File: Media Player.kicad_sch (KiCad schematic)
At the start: 1 part, among them U1 ESP32-S3-WROOM-1

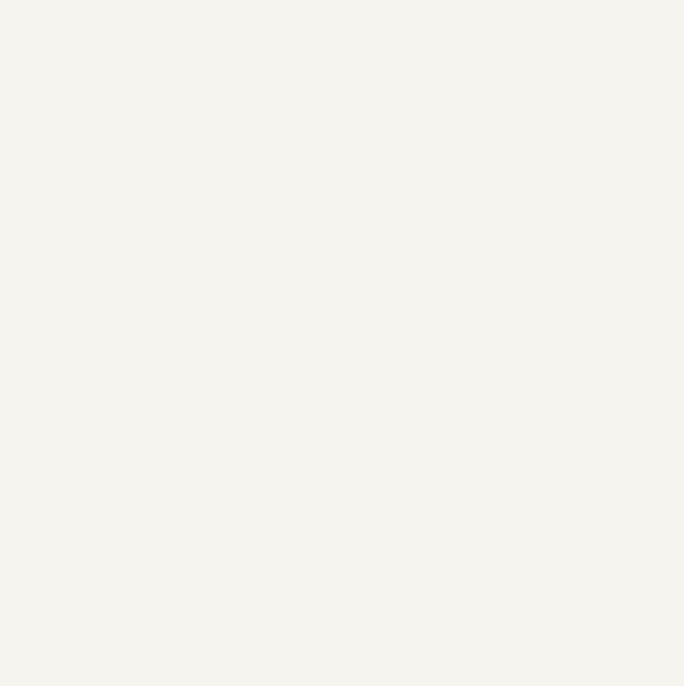
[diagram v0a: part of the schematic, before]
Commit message: Added Power sub page.
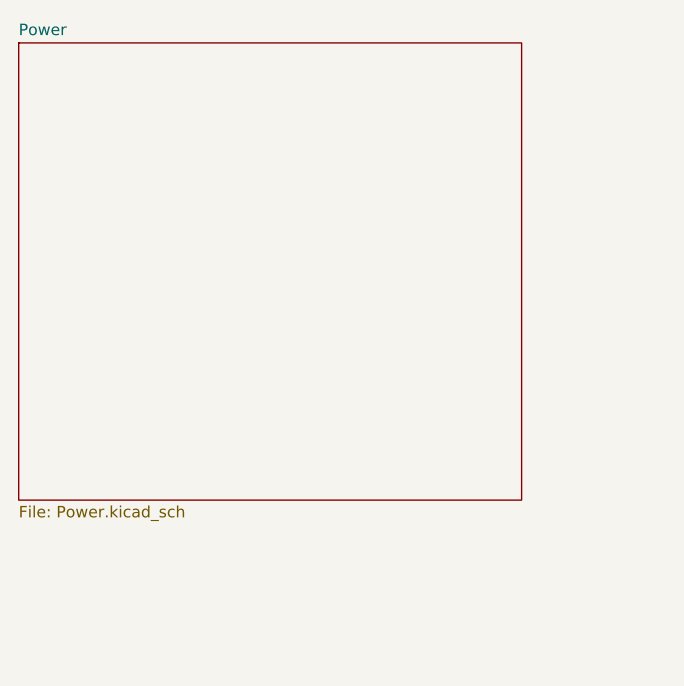
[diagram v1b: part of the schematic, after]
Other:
- added sheet Power (Power.kicad_sch)
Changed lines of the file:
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@@
+		)
+	)
+	(sheet
+		(at 20.32 17.78)
+		(size 55.88 50.8)
+		(exclude_from_sim no)
+		(in_bom yes)
+		(on_board yes)
+		(dnp no)
+		(fields_autoplaced yes)
+		(stroke
+			(width 0.1524)
+			(type solid)
+		)
+		(fill
+			(color 255 248 184 1.0000)
+		)
+		(property "Sheetname" "Power"
+			(at 20.32 17.0684 0)
+			(effects
+				(font
+					(size 1.27 1.27)
+				)
+				(justify left bottom)
+			)
+		)
+		(property "Sheetfile" "Power.kicad_sch"
+			(at 20.32 69.1646 0)
+			(effects
+				(font
+					(size 1.27 1.27)
+				)
+				(justify left top)
+			)
+		)
+		(instances
+			(project "Media Player"
+				(path "/5c19345b-3707-4c90-b593-78a9c3e56866"
+					(page "2")
+				)
+			)
 		)
 	)

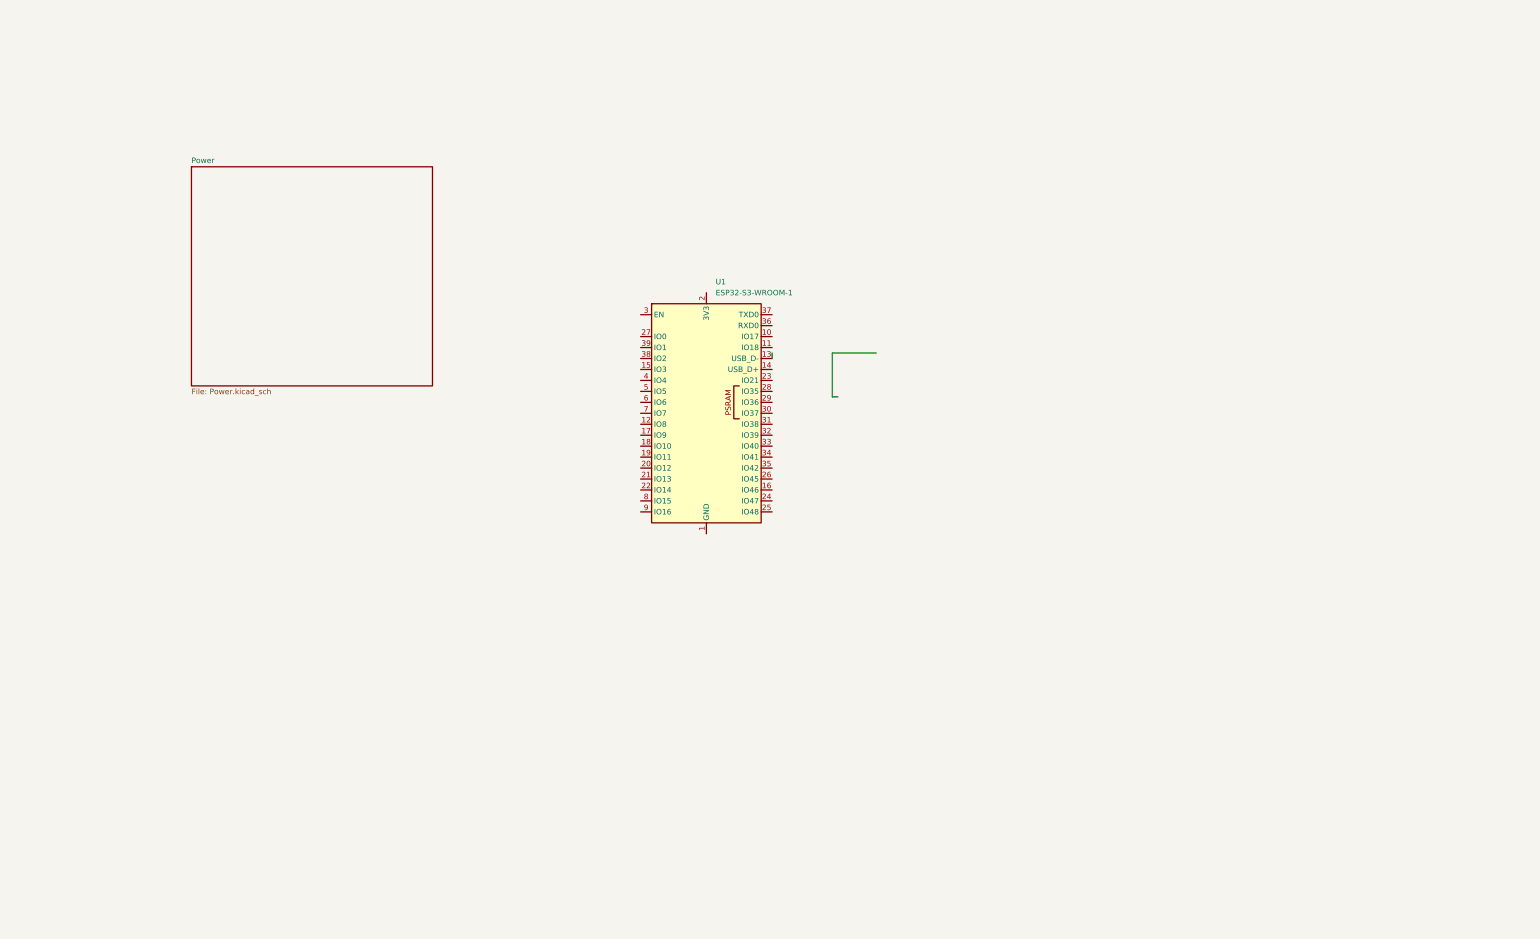
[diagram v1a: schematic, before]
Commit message: Placed Major Components, No Power
Placed ESP32S3, Connector to LCD, SD card reader, USB. Audio Jack components still tbd. Power is a hierarchical page/symbol, no pins right now.
Note to self: KiCAD will crash if you try to edit symbols by double clicking on them inside a schematic. Use symbol editor instead.
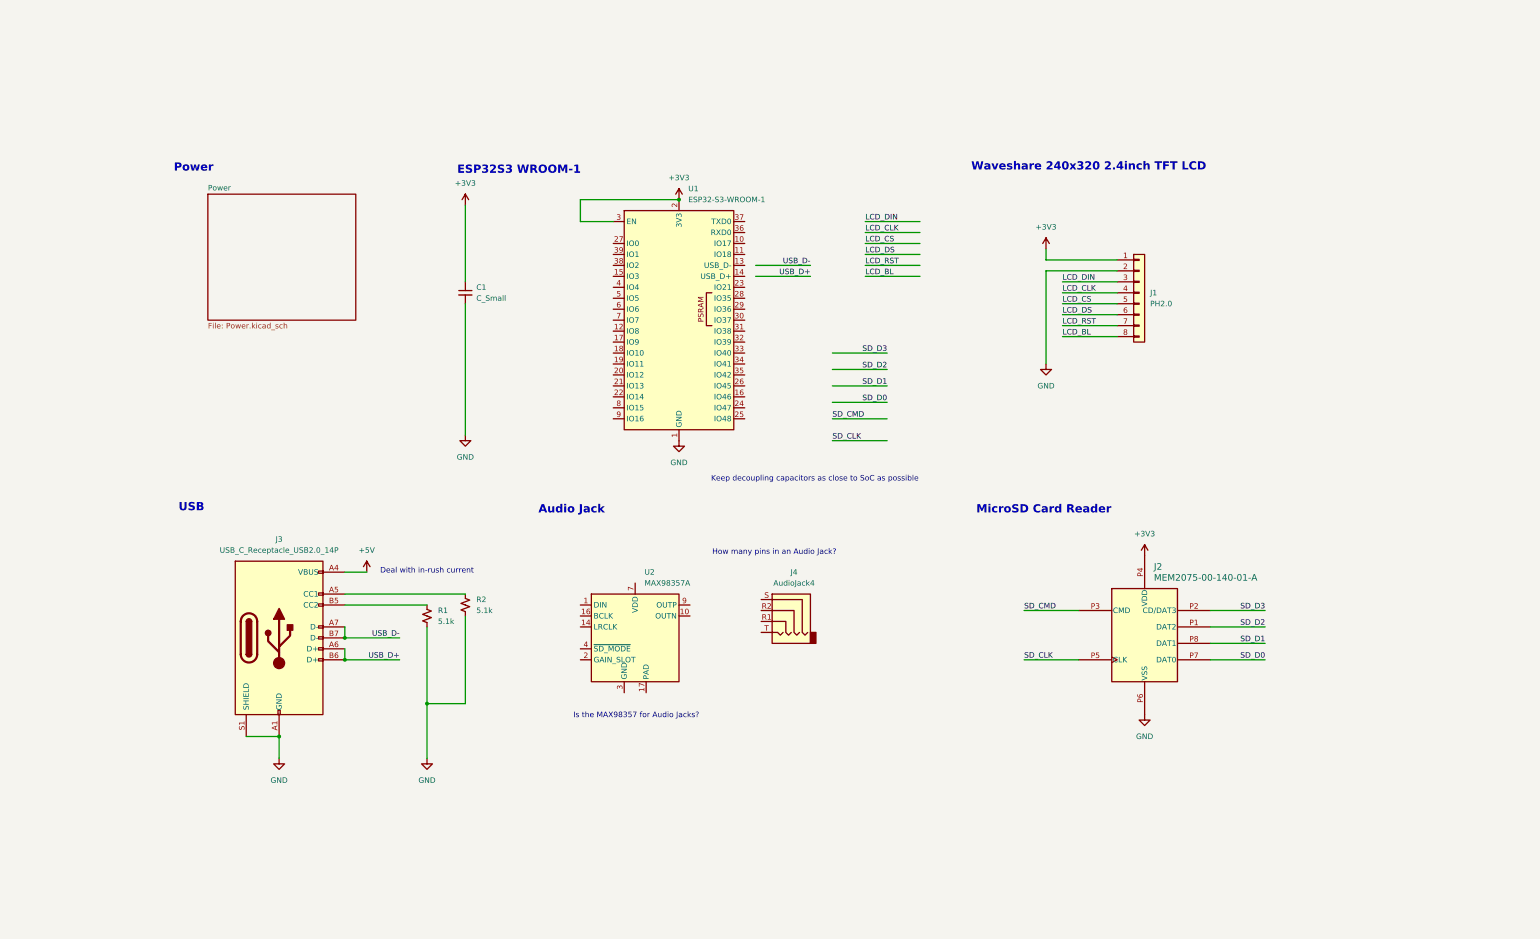
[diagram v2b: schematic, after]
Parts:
- added C1: C_Small, symbol Device:C_Small
- added J1: PH2.0, symbol Connector_Generic:Conn_01x08
- added J2: MEM2075-00-140-01-A, MEM2075-00-140-01-A_GCT, symbol MEM2075:MEM2075-00-140-01-A
- added J3: USB_C_Receptacle_USB2.0_14P, symbol Connector:USB_C_Receptacle_USB2.0_14P
- added J4: AudioJack4, symbol Connector_Audio:AudioJack4
- added R1, R2: 5.1k, symbol Device:R_Small_US
- added U2: MAX98357A, Package_DFN_QFN:TQFN-16-1EP_3x3mm_P0.5mm_EP1.23x1.23mm, symbol Audio:MAX98357A
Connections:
- net GND: now reaches U1.1 (GND), U1.40 (GND), U1.41 (GND)
- net GND: now also C1.2, J1.2 (Pin_2), J2.P6 (VSS), J3.A1 (GND), J3.A12 (GND), J3.B1 (GND), J3.B12 (GND), J3.S1 (SHIELD), R1.2, R2.2
- net +3V3: now reaches U1.2 (3V3)
- net +3V3: now also U1.3 (EN), C1.1, J1.1 (Pin_1), J2.P4 (VDD)
- new net: J3.B5 (CC2), R1.1
- new net: U2.11 (GND), U2.15 (GND), U2.3 (GND)
- new net: U2.7 (VDD), U2.8 (VDD)
- new net: J3.A5 (CC1), R2.1
- new net +5V: J3.A4 (VBUS), J3.A9 (VBUS), J3.B4 (VBUS), J3.B9 (VBUS)
- new net LCD_BL: J1.8 (Pin_8)
- new net LCD_CLK: J1.4 (Pin_4)
- new net LCD_CS: J1.5 (Pin_5)
- new net LCD_DIN: J1.3 (Pin_3)
- new net LCD_DS: J1.6 (Pin_6)
- new net LCD_RST: J1.7 (Pin_7)
- new net SD_CLK: J2.P5 (CLK)
- new net SD_CMD: J2.P3 (CMD)
- new net SD_D0: J2.P7 (DAT0)
- new net SD_D1: J2.P8 (DAT1)
- new net SD_D2: J2.P1 (DAT2)
- new net SD_D3: J2.P2 (CD/DAT3)
- new net USB_D+: J3.A6 (D+), J3.B6 (D+)
- new net USB_D-: J3.A7 (D-), J3.B7 (D-)
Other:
- note added: "Audio Jack"
- note added: "Deal with in-rush current"
- note added: "ESP32S3 WROOM-1"
- note added: "How many pins in an Audio Jack?"
- note added: "Is the MAX98357 for Audio Jacks?"
- note added: "Keep decoupling capacitors as close to SoC as possible"
- note added: "MicroSD Card Reader"
- note added: "Power"
- note added: "USB"
- note added: "Waveshare 240x320 2.4inch TFT LCD"
- moved on the sheet: U1

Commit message: Most connections formed except component values and audio amp
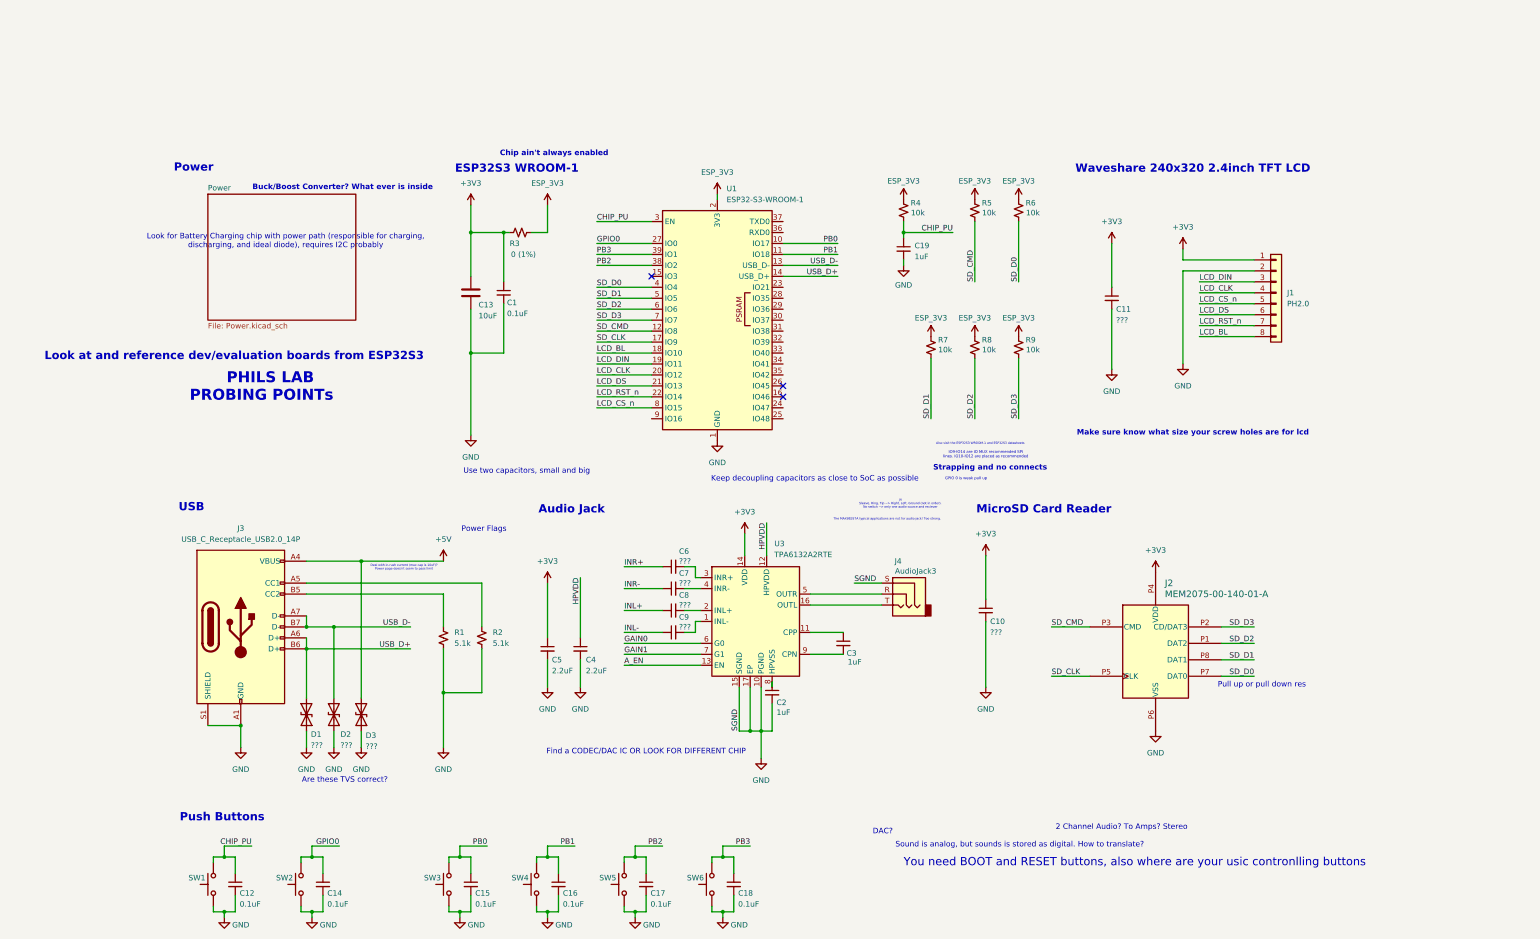
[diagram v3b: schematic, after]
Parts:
- removed J4: AudioJack4, symbol Connector_Audio:AudioJack4
- removed U2: MAX98357A, Package_DFN_QFN:TQFN-16-1EP_3x3mm_P0.5mm_EP1.23x1.23mm, symbol Audio:MAX98357A
- added C10, C11, C6, C7, C8, C9: ???, symbol Device:C_Small
- added C12, C14, C15, C16, C17, C18: 0.1uF, symbol Device:C_Small
- added C13: 10uF, symbol Device:C
- added C19, C2, C3: 1uF, symbol Device:C_Small
- added C4, C5: 2.2uF, symbol Device:C_Small
- added D1, D2, D3: ???, Diode_THT:D_DO-201AE_P15.24mm_Horizontal, symbol Diode:1.5KExxCA
- added J4: AudioJack3, symbol Connector_Audio:AudioJack3
- added R3: 0 (1%), symbol Device:R_Small_US
- added R4, R5, R6, R7, R8, R9: 10k, symbol Device:R_Small_US
- added SW1, SW2, SW3, SW4, SW5, SW6: SW_Push, symbol Switch:SW_Push
- added U3: TPA6132A2RTE, Package_DFN_QFN:WQFN-16-1EP_3x3mm_P0.5mm_EP1.6x1.6mm_ThermalVias, symbol Amplifier_Audio:TPA6132A2RTE
- C1: value C_Small -> 0.1uF
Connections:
- net LCD_CS is gone; now on net LCD_CS_n: J1.5 (Pin_5)
- net LCD_RST is gone; now on net LCD_RST_n: J1.7 (Pin_7)
- net +3V3: now also C10.1, C11.1, C13.1, C5.1, R3.1, U3.14 (VDD); no longer U1.2 (3V3), U1.3 (EN)
- net +5V: now also D3.2 (A2)
- net GND: now also C10.2, C11.2, C12.2, C13.2, C14.2, C15.2, C16.2, C17.2, C18.2, C19.2, C2.2, C4.2, C5.2, D1.1 (A1), D2.1 (A1), D3.1 (A1), J4.S, SW1.1, SW2.1, SW3.1, SW4.1, SW5.1, SW6.1, U3.10 (PGND), U3.15 (SGND), U3.17 (EP)
- net LCD_BL: now also U1.18 (IO10)
- net LCD_CLK: now also U1.20 (IO12)
- net LCD_DIN: now also U1.19 (IO11)
- net LCD_DS: now also U1.21 (IO13)
- net SD_CLK: now also U1.17 (IO9)
- net SD_CMD: now also U1.12 (IO8), R5.1
- net SD_D0: now also U1.4 (IO4), R6.1
- net SD_D1: now also U1.5 (IO5), R7.1
- net SD_D2: now also U1.6 (IO6), R8.1
- net SD_D3: now also U1.7 (IO7), R9.1
- net USB_D+: now also U1.14 (USB_D+), D1.2 (A2)
- net USB_D-: now also U1.13 (USB_D-), D2.2 (A2)
- net PB0: now reaches U1.10 (IO17)
- net PB0: now also C15.1, SW3.2
- net PB1: now reaches U1.11 (IO18)
- net PB1: now also C16.1, SW4.2
- net LCD_RST_n: now reaches U1.22 (IO14)
- net GPIO0: now reaches U1.27 (IO0)
- net GPIO0: now also C14.1, SW2.2
- net PB2: now reaches U1.38 (IO2)
- net PB2: now also C17.1, SW5.2
- net PB3: now reaches U1.39 (IO1)
- net PB3: now also C18.1, SW6.2
- net LCD_CS_n: now reaches U1.8 (IO15)
- new net: C3.1, U3.11 (CPP)
- new net: C3.2, U3.9 (CPN)
- new net: C9.2, U3.1 (INL-)
- new net: J4.T, U3.16 (OUTL)
- new net: C8.2, U3.2 (INL+)
- new net: C6.2, U3.3 (INR+)
- new net: C7.2, U3.4 (INR-)
- new net: J4.R, U3.5 (OUTR)
- new net: C2.1, U3.8 (HPVSS)
- new net A_EN: U3.13 (EN)
- new net CHIP_PU: C12.1, C19.1, R4.1, SW1.2, U1.3 (EN)
- new net ESP_3V3: R3.2, R4.2, R5.2, R6.2, R7.2, R8.2, R9.2, U1.2 (3V3)
- new net GAIN0: U3.6 (G0)
- new net GAIN1: U3.7 (G1)
- new net HPVDD: C4.1, U3.12 (HPVDD)
- new net INL+: C8.1
- new net INL-: C9.1
- new net INR+: C6.1
- new net INR-: C7.1
- no-connect marks 0 -> 3
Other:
- note added: "2 Channel Audio? To Amps? Stereo"
- note added: "Also visit the ESP32S3 WROOM-1 and ESP32S3 datasheets"
- note added: "Are these TVS correct?"
- note added: "Buck/Boost Converter? What ever is inside"
- note added: "Chip ain't always enabled"
- note added: "DAC?"
- note added: "Deal with in-rush current (max cap is 10uF)? Power page doesn't seem to pass limit"
- note added: "Find a CODEC/DAC IC OR LOOK FOR DIFFERENT CHIP"
- note added: "GPIO 0 is weak pull up"
- note added: "IO9-IO14 are IO MUX recommended SPI lines. IO10-IO12 are placed as recommended"
- note added: "J4 Sleeve, Ring, Tip --> Right, Left, Ground (not in order). No switch --> only one audio source and reciever"
- note added: "Look at and reference dev/evaluation boards from ESP32S3"
- note added: "Look for Battery Charging chip with power path (responsible for charging, discharging, and ideal diode), requires I2C probably"
- note added: "Make sure know what size your screw holes are for lcd"
- note added: "PHILS LAB"
- note added: "PROBING POINTs"
- note added: "Power Flags"
- note added: "Pull up or pull down res"
- note added: "Push Buttons"
- note added: "Sound is analog, but sounds is stored as digital. How to translate?"
- note added: "Strapping and no connects"
- note added: "The MAX98357A typical applications are not for audio jack! Too strong."
- note added: "Use two capacitors, small and big"
- note added: "You need BOOT and RESET buttons, also where are your usic contronlling buttons"
- note removed: "Deal with in-rush current"
- note removed: "How many pins in an Audio Jack?"
- note removed: "Is the MAX98357 for Audio Jacks?"
- moved on the sheet: C1, J1, J2, J3, R1, R2, U1

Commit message: Changed Audio Amplifier to MAX9850
MAX9850 is so complicated - you use I2C to set the internal registers to modify and initialize the IC before you use I2S to send audio data to DAC. You can also choose to send analog data with AC coupling capacitors. Output can go to speaker and headphone jack. Very versatile, extremely annoying reading a 36 page data sheet for 2 hours. No power yet.
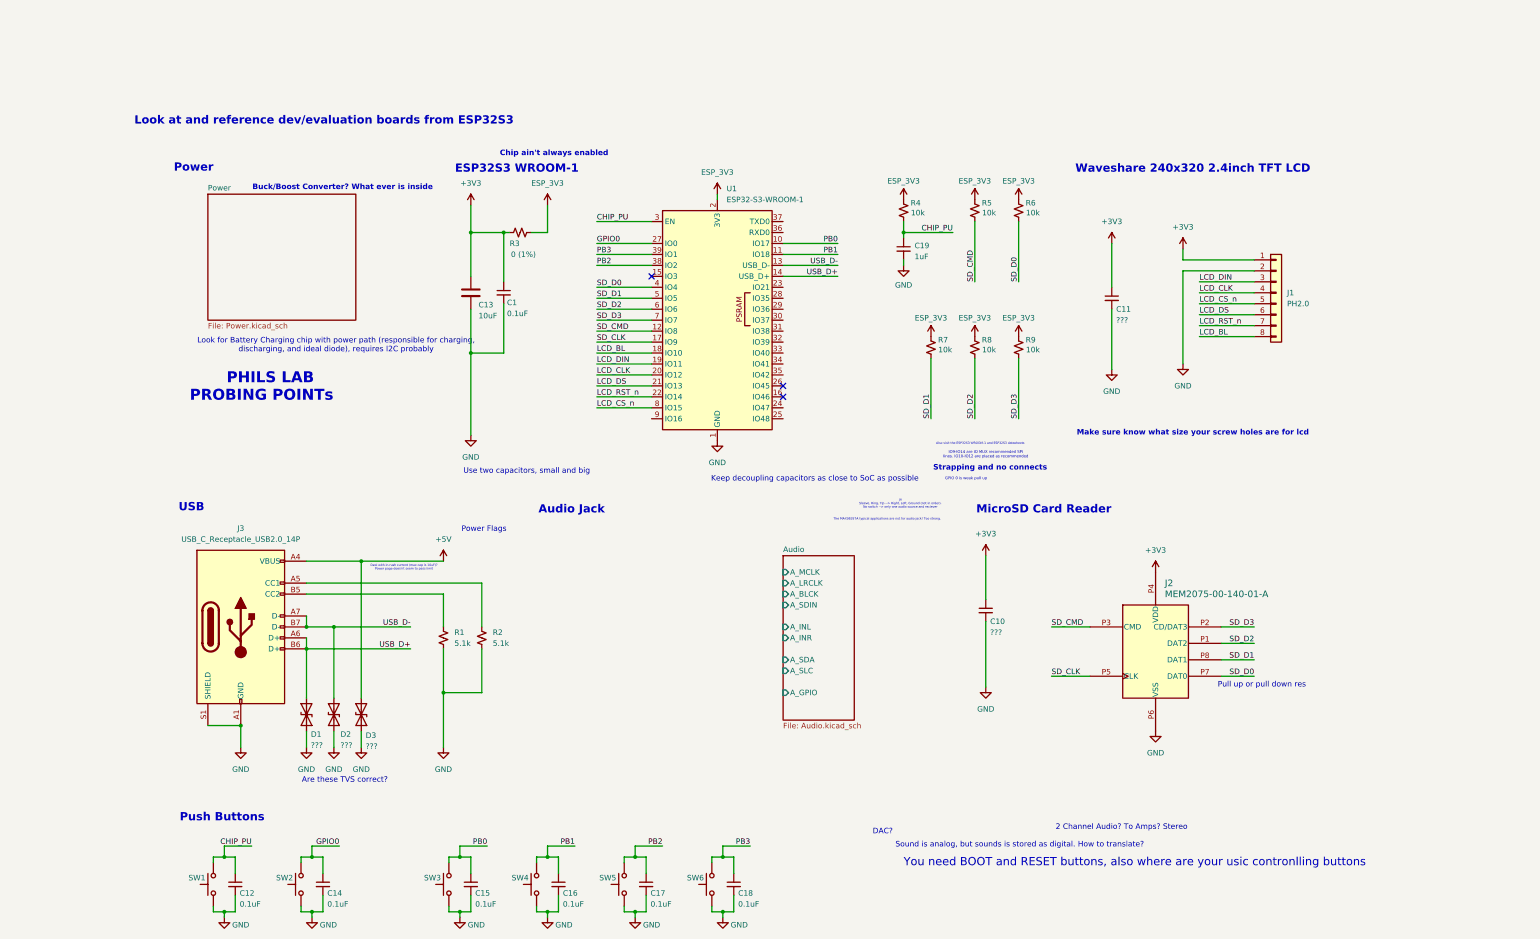
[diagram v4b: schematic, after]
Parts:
- removed C2, C3: 1uF, symbol Device:C_Small
- removed C4, C5: 2.2uF, symbol Device:C_Small
- removed C6, C7, C8, C9: ???, symbol Device:C_Small
- removed J4: AudioJack3, symbol Connector_Audio:AudioJack3
- removed U3: TPA6132A2RTE, Package_DFN_QFN:WQFN-16-1EP_3x3mm_P0.5mm_EP1.6x1.6mm_ThermalVias, symbol Amplifier_Audio:TPA6132A2RTE
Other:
- added sheet Audio (Audio.kicad_sch)
- note removed: "Find a CODEC/DAC IC OR LOOK FOR DIFFERENT CHIP"
